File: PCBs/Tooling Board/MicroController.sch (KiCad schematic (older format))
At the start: 21 parts

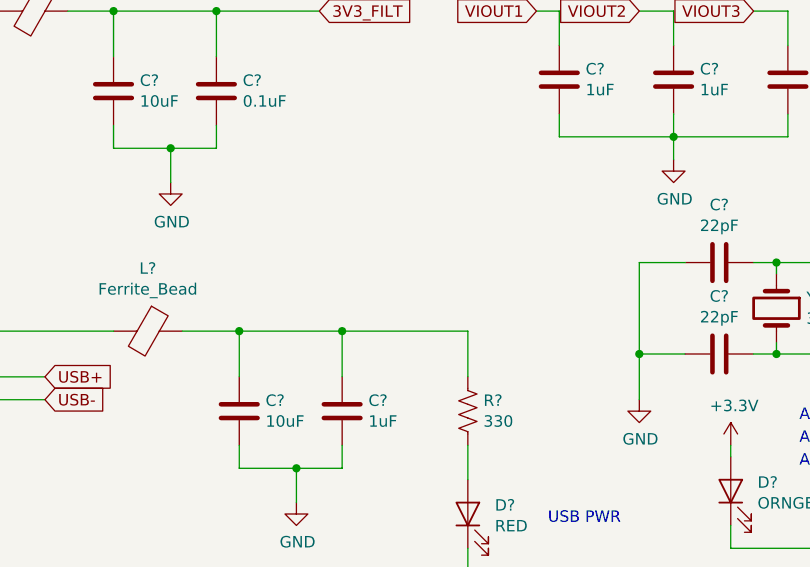
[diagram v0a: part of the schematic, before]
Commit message: Add DC Motor Control
-Added H-bridge drivers and logic inverters
-Should be able to control up to 6 DC motors / other loads
-We'll see if we can fit 3 chips on the board (we should be able to)
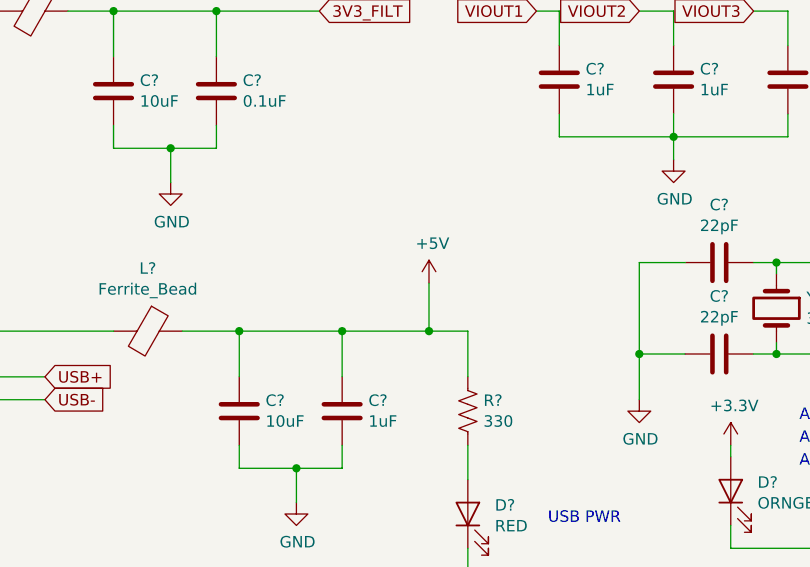
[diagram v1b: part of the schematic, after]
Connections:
- net +5V: now also C?.1, C?.1, L?.1, R?.1
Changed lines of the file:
@@
 $Descr A4 11693 8268
 encoding utf-8
-Sheet 2 4
+Sheet 2 7
 Title ""
 Date ""
@@
 Connection ~ 3250 2500
 Wire Wire Line
-	3250 2500 3800 2500
+	3250 2500 3630 2500
 Connection ~ 2800 2500
 Wire Wire Line
@@
 Text GLabel 5800 2850 0    50   Input ~ 0
 VIOUT1
+$Comp
+L power:+5V #PWR?
+U 1 1 5C4C3747
+P 3630 2290
+F 0 "#PWR?" H 3630 2140 50  0001 C CNN
+F 1 "+5V" H 3645 2463 50  0000 C CNN
+F 2 "" H 3630 2290 50  0001 C CNN
+F 3 "" H 3630 2290 50  0001 C CNN
+	1    3630 2290
+	1    0    0    -1
+$EndComp
+Wire Wire Line
+	3630 2290 3630 2500
+Connection ~ 3630 2500
+Wire Wire Line
+	3630 2500 3800 2500
 $EndSCHEMATC

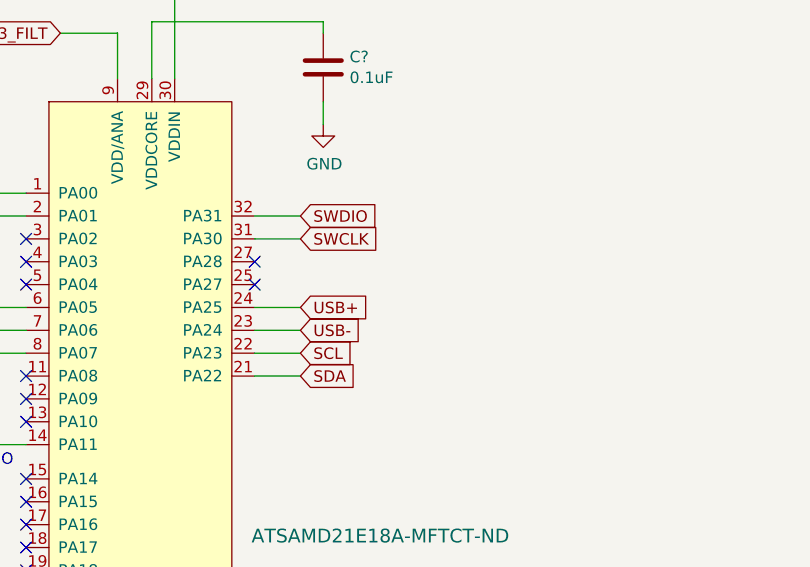
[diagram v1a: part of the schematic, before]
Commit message: Added Sensors
-Added pH Circuit and spec'd components
-Added Pressure sensor connecter
-Added External Temp sensor connector
-Added metal detector connector + input circuit

Need to add IMU interface now (not hard)
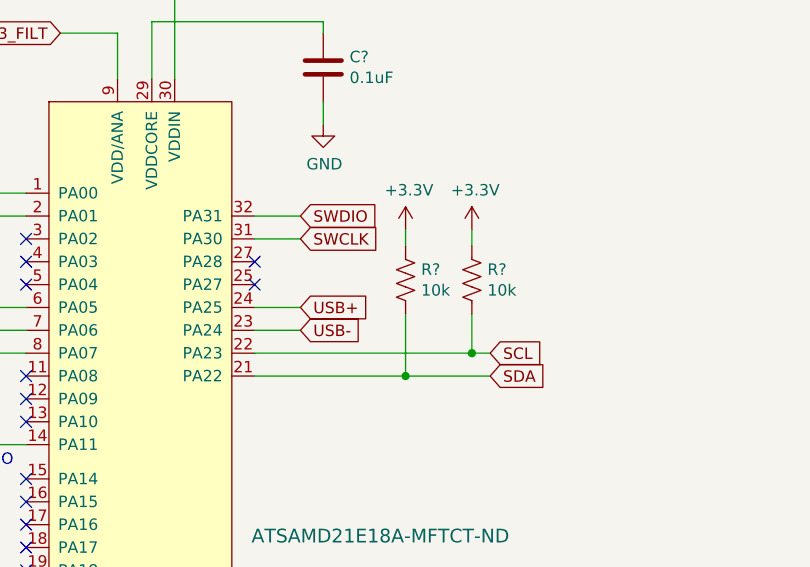
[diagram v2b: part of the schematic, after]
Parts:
- added R? (x2): 10k, symbol Device:R_US
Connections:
- net +3V3: now also R?.1, R?.1
- net SCL: now also R?.2
- net SDA: now also R?.2
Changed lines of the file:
@@
 $Descr A4 11693 8268
 encoding utf-8
-Sheet 2 7
+Sheet 2 8
 Title ""
 Date ""
@@
 	6000 3050 5800 3050
 Wire Wire Line
-	7000 3150 7200 3150
+	7000 3150 7660 3150
 Wire Wire Line
-	7000 3050 7200 3050
-Text GLabel 7200 3150 2    50   Input ~ 0
+	7000 3050 7950 3050
+Text GLabel 8030 3150 2    50   Input ~ 0
 SDA
-Text GLabel 7200 3050 2    50   Input ~ 0
+Text GLabel 8030 3050 2    50   Input ~ 0
 SCL
 $Comp
@@
 Wire Wire Line
 	3630 2500 3800 2500
+Wire Wire Line
+	7660 3150 7660 2880
+Connection ~ 7660 3150
+Wire Wire Line
+	7660 3150 8030 3150
+Wire Wire Line
+	7950 3050 7950 2880
+Connection ~ 7950 3050
+Wire Wire Line
+	7950 3050 8030 3050
+$Comp
+L Device:R_US R?
+U 1 1 5C4EC3B3
+P 7660 2730
+F 0 "R?" H 7728 2776 50  0000 L CNN
+F 1 "10k" H 7728 2685 50  0000 L CNN
+F 2 "" V 7700 2720 50  0001 C CNN
+F 3 "" H 7660 2730 50  0001 C CNN
+	1    7660 2730
+	1    0    0    -1
+$EndComp
+$Comp
+L Device:R_US R?
+U 1 1 5C4F7260
+P 7950 2730
+F 0 "R?" H 8018 2776 50  0000 L CNN
+F 1 "10k" H 8018 2685 50  0000 L CNN
+F 2 "" V 7990 2720 50  0001 C CNN
+F 3 "" H 7950 2730 50  0001 C CNN
+	1    7950 2730
+	1    0    0    -1
+$EndComp
+$Comp
+L power:+3.3V #PWR?
+U 1 1 5C4F72E4
+P 7660 2510
+F 0 "#PWR?" H 7660 2360 50  0001 C CNN
+F 1 "+3.3V" H 7675 2683 50  0000 C CNN
+F 2 "" H 7660 2510 50  0001 C CNN
+F 3 "" H 7660 2510 50  0001 C CNN
+	1    7660 2510
+	1    0    0    -1
+$EndComp
+$Comp
+L power:+3.3V #PWR?
+U 1 1 5C4F73BE
+P 7950 2510
+F 0 "#PWR?" H 7950 2360 50  0001 C CNN
+F 1 "+3.3V" H 7965 2683 50  0000 C CNN
+F 2 "" H 7950 2510 50  0001 C CNN
+F 3 "" H 7950 2510 50  0001 C CNN
+	1    7950 2510
+	1    0    0    -1
+$EndComp
+Wire Wire Line
+	7950 2580 7950 2510
+Wire Wire Line
+	7660 2580 7660 2510
 $EndSCHEMATC

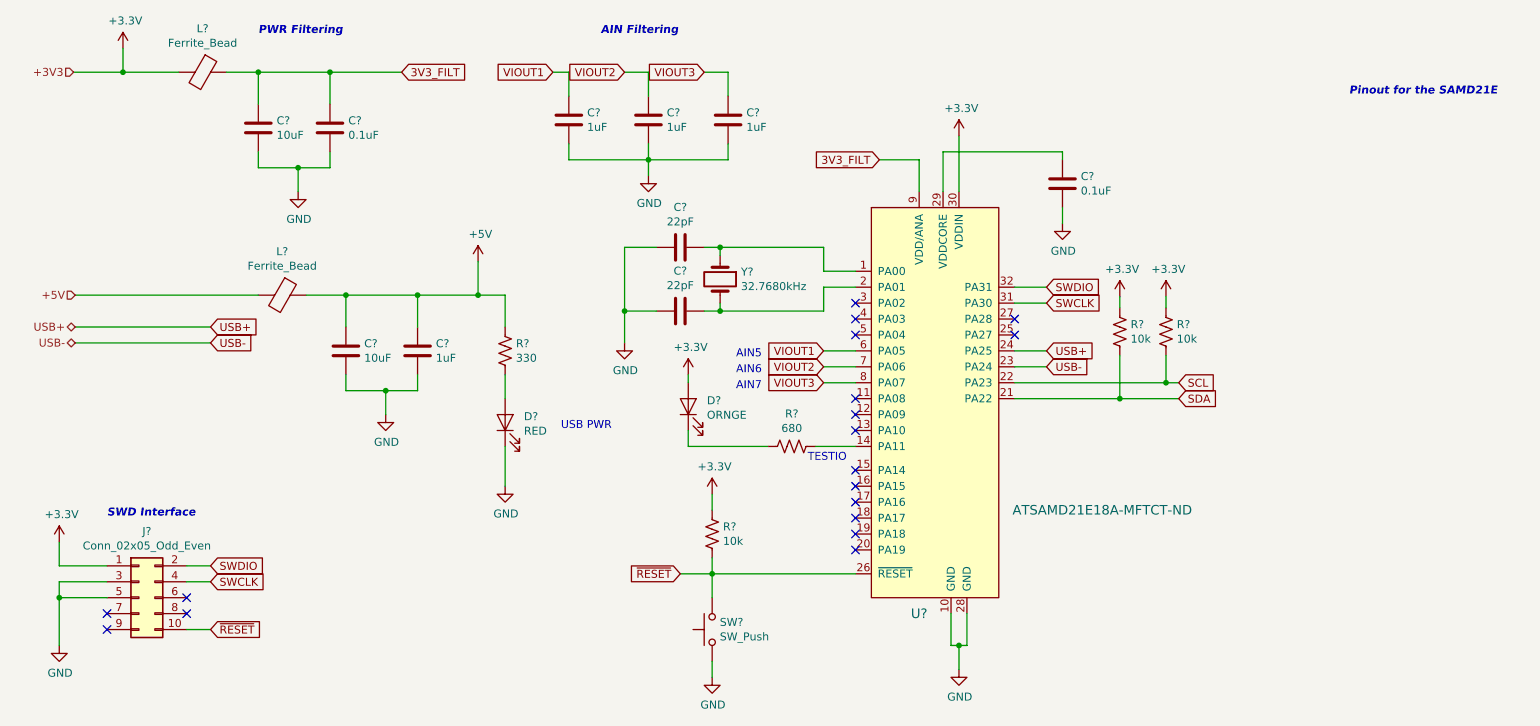
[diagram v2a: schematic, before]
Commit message: Pins are Mapped
-This was really difficult and it may not work.
-We're gonna try it and see what works.
-If it fails the next PCB will use arduino atmega chips since the open source libraries exist for them
-Might do a combination of SAMD and atmega lol
-God damn chinese new year
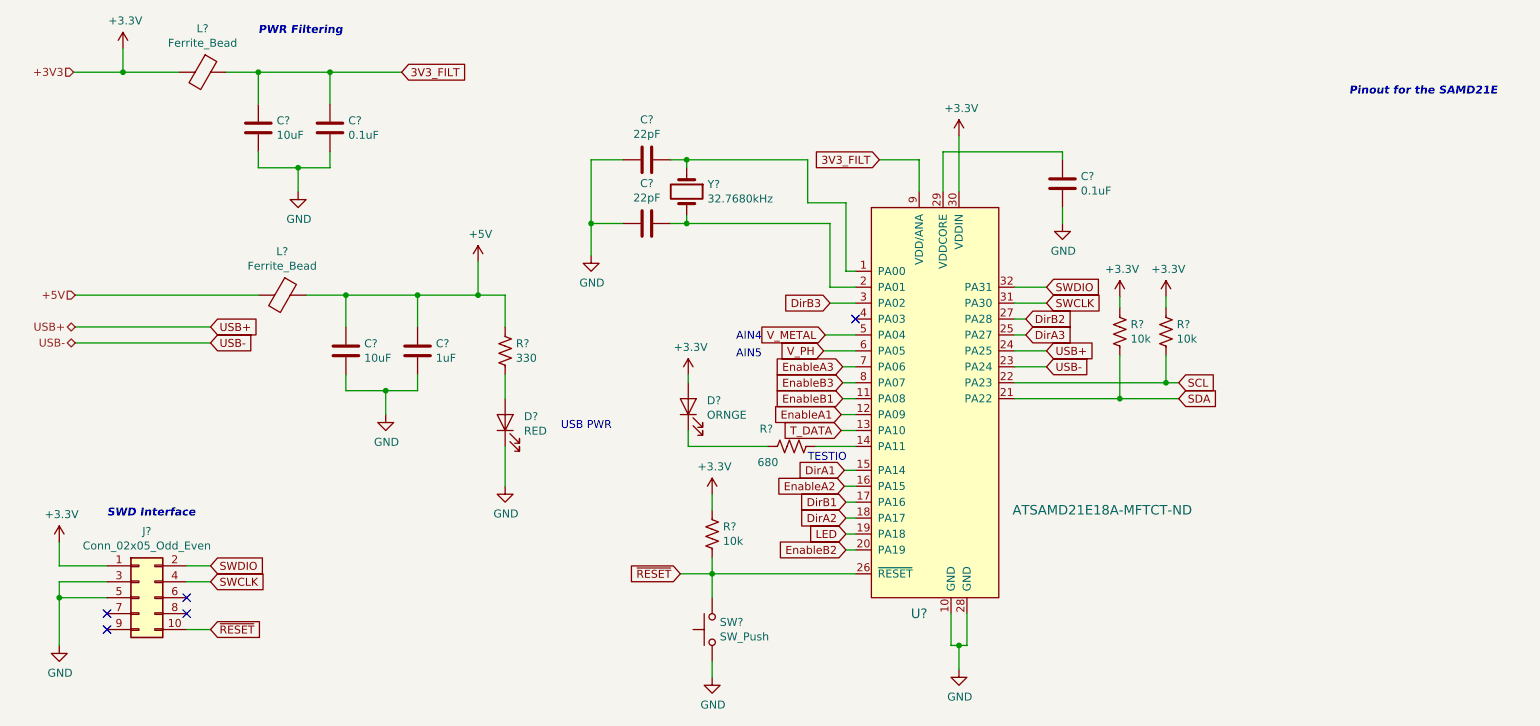
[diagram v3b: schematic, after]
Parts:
- removed C? (x3): 1uF, Capacitors_SMD:C_0603, symbol Device:C
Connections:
- net EnableB1: now reaches U?.11 (PA08)
- net EnableA1: now reaches U?.12 (PA09)
- net T_DATA: now reaches U?.13 (PA10)
- net DirA1: now reaches U?.15 (PA14)
- net EnableA2: now reaches U?.16 (PA15)
- net DirB1: now reaches U?.17 (PA16)
- net DirA2: now reaches U?.18 (PA17)
- net LED: now reaches U?.19 (PA18)
- net EnableB2: now reaches U?.20 (PA19)
- net DirA3: now reaches U?.25 (PA27)
- net DirB2: now reaches U?.27 (PA28)
- net DirB3: now reaches U?.3 (PA02)
- net V_METAL: now reaches U?.5 (PA04)
- net VIOUT1 renamed V_PH
- net VIOUT2 renamed EnableA3
- net VIOUT3 renamed EnableB3
- no-connect marks 18 -> 5
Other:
- note added: "AIN4"
- note removed: "AIN Filtering\n\n"
- note removed: "AIN6"
- note removed: "AIN7"
- moved on the sheet: C?, Y?
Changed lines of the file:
@@
 EESchema Schematic File Version 4
-LIBS:Actuator Board-cache
+LIBS:Tooling Board-cache
 EELAYER 26 0
 EELAYER END
@@
 Comment4 ""
 $EndDescr
-$Comp
-L EER:ATSAMD21E18A-MFT U?
-U 1 1 5BCD2DFE
-P 6500 3450
-F 0 "U?" H 6400 2400 60  0000 C CNN
-F 1 "ATSAMD21E18A-MFTCT-ND" H 7550 3050 60  0000 C CNN
-F 2 "EER:QFN-32-1EP_5x5mm" H 7900 3550 60  0001 L CNN
-F 3 "ATSAMD21E18A-MFTCT-ND" H 7900 3650 60  0001 L CNN
-F 4 "Active" H 6700 4650 60  0001 L CNN "Status"
-	1    6500 3450
-	1    0    0    -1
-$EndComp
 $Bitmap
 Pos 9600 3100
@@
 L Device:Crystal Y?
 U 1 1 5BDACFC8
-P 5150 2400
-F 0 "Y?" V 5104 2531 50  0000 L CNN
-F 1 "32.7680kHz" V 5195 2531 50  0000 L CNN
-F 2 "EER:Crystal_SMD_3215-2pin_3.2x1.5mm" H 5150 2400 50  0001 C CNN
-F 3 "887-2605-1-ND" H 5150 2400 50  0001 C CNN
-	1    5150 2400
+P 4940 1850
+F 0 "Y?" V 4894 1981 50  0000 L CNN
+F 1 "32.7680kHz" V 4985 1981 50  0000 L CNN
+F 2 "EER:Crystal_SMD_3215-2pin_3.2x1.5mm" H 4940 1850 50  0001 C CNN
+F 3 "887-2605-1-ND" H 4940 1850 50  0001 C CNN
+	1    4940 1850
 	0    1    1    0
 $EndComp
@@
 L Device:C C?
 U 1 1 5BDAD072
-P 4900 2200
-F 0 "C?" V 4648 2200 50  0000 C CNN
-F 1 "22pF" V 4739 2200 50  0000 C CNN
-F 2 "Capacitors_SMD:C_0603" H 4938 2050 50  0001 C CNN
-F 3 "311-3925-1-ND" H 4900 2200 50  0001 C CNN
-	1    4900 2200
+P 4690 1650
+F 0 "C?" V 4438 1650 50  0000 C CNN
+F 1 "22pF" V 4529 1650 50  0000 C CNN
+F 2 "Capacitors_SMD:C_0603" H 4728 1500 50  0001 C CNN
+F 3 "311-3925-1-ND" H 4690 1650 50  0001 C CNN
+	1    4690 1650
 	0    1    1    0
 $EndComp
@@
 L Device:C C?
 U 1 1 5BDAD111
-P 4900 2600
-F 0 "C?" V 4648 2600 50  0000 C CNN
-F 1 "22pF" V 4739 2600 50  0000 C CNN
-F 2 "Capacitors_SMD:C_0603" H 4938 2450 50  0001 C CNN
-F 3 "311-3925-1-ND" H 4900 2600 50  0001 C CNN
-	1    4900 2600
+P 4690 2050
+F 0 "C?" V 4438 2050 50  0000 C CNN
+F 1 "22pF" V 4529 2050 50  0000 C CNN
+F 2 "Capacitors_SMD:C_0603" H 4728 1900 50  0001 C CNN
+F 3 "311-3925-1-ND" H 4690 2050 50  0001 C CNN
+	1    4690 2050
 	0    1    1    0
 $EndComp
 Wire Wire Line
-	5050 2200 5150 2200
-Wire Wire Line
-	5150 2200 5150 2250
-Wire Wire Line
-	5150 2550 5150 2600
-Wire Wire Line
-	5150 2600 5050 2600
-Wire Wire Line
-	5150 2200 5800 2200
-Wire Wire Line
-	5800 2200 5800 2350
+	4840 1650 4940 1650
 Wire Wire Line
-	5800 2350 6000 2350
-Connection ~ 5150 2200
+	4940 1650 4940 1700
 Wire Wire Line
-	6000 2450 5800 2450
+	4940 2000 4940 2050
 Wire Wire Line
-	5800 2450 5800 2600
+	4940 2050 4840 2050
+Connection ~ 4940 1650
+Connection ~ 4940 2050
 Wire Wire Line
-	5800 2600 5150 2600
-Connection ~ 5150 2600
+	4540 1650 4340 1650
 Wire Wire Line
-	4750 2200 4550 2200
+	4340 1650 4340 2050
 Wire Wire Line
-	4550 2200 4550 2600
+	4340 2050 4540 2050
 Wire Wire Line
-	4550 2600 4750 2600
-Wire Wire Line
-	4550 2600 4550 2800
-Connection ~ 4550 2600
+	4340 2050 4340 2250
+Connection ~ 4340 2050
 $Comp
 L power:GND #PWR?
 U 1 1 5BDB1CC8
-P 4550 2800
-F 0 "#PWR?" H 4550 2550 50  0001 C CNN
-F 1 "GND" H 4555 2627 50  0000 C CNN
-F 2 "" H 4550 2800 50  0001 C CNN
-F 3 "" H 4550 2800 50  0001 C CNN
-	1    4550 2800
+P 4340 2250
+F 0 "#PWR?" H 4340 2000 50  0001 C CNN
+F 1 "GND" H 4345 2077 50  0000 C CNN
+F 2 "" H 4340 2250 50  0001 C CNN
+F 3 "" H 4340 2250 50  0001 C CNN
+	1    4340 2250
 	1    0    0    -1
 $EndComp
@@
 	6000 2850 5800 2850
 Wire Wire Line
-	6000 2950 5800 2950
-Wire Wire Line
-	6000 3050 5800 3050
-Wire Wire Line
 	7000 3150 7660 3150
 Wire Wire Line
@@
 U 1 1 5BDD760F
 P 5600 3450
-F 0 "R?" V 5395 3450 50  0000 C CNN
-F 1 "680" V 5486 3450 50  0000 C CNN
+F 0 "R?" V 5490 3290 50  0000 C CNN
+F 1 "680" V 5700 3300 50  0000 C CNN
 F 2 "Resistors_SMD:R_0603" V 5640 3440 50  0001 C CNN
 F 3 "RHM680DCT-ND" H 5600 3450 50  0001 C CNN
@@
 Wire Wire Line
 	5100 4250 6000 4250
-NoConn ~ 6000 2550
-NoConn ~ 6000 2650
-NoConn ~ 6000 2750
-NoConn ~ 6000 3150
-NoConn ~ 6000 3250
-NoConn ~ 6000 3350
-NoConn ~ 6000 3600
-NoConn ~ 6000 3700
-NoConn ~ 6000 3800
-NoConn ~ 6000 4000
-NoConn ~ 6000 3900
-NoConn ~ 6000 4100
-NoConn ~ 7000 2750
-NoConn ~ 7000 2650
 Text Notes 2250 950  0    50   Italic 10
 PWR Filtering\n\n
@@
 NoConn ~ 1300 4500
 NoConn ~ 1300 4600
-$Comp
-L Device:C C?
-U 1 1 5BE103F1
-P 4200 1400
-F 0 "C?" H 4315 1446 50  0000 L CNN
-F 1 "1uF" H 4315 1355 50  0000 L CNN
-F 2 "Capacitors_SMD:C_0603" H 4238 1250 50  0001 C CNN
-F 3 "1276-6524-1-ND" H 4200 1400 50  0001 C CNN
-	1    4200 1400
-	1    0    0    -1
-$EndComp
-$Comp
-L Device:C C?
-U 1 1 5BE1047D
-P 4700 1400
-F 0 "C?" H 4815 1446 50  0000 L CNN
-F 1 "1uF" H 4815 1355 50  0000 L CNN
-F 2 "Capacitors_SMD:C_0603" H 4738 1250 50  0001 C CNN
-F 3 "1276-6524-1-ND" H 4700 1400 50  0001 C CNN
-	1    4700 1400
-	1    0    0    -1
-$EndComp
-$Comp
-L Device:C C?
-U 1 1 5BE104C5
-P 5200 1400
-F 0 "C?" H 5315 1446 50  0000 L CNN
-F 1 "1uF" H 5315 1355 50  0000 L CNN
-F 2 "Capacitors_SMD:C_0603" H 5238 1250 50  0001 C CNN
-F 3 "1276-6524-1-ND" H 5200 1400 50  0001 C CNN
-	1    5200 1400
-	1    0    0    -1
-$EndComp
-Wire Wire Line
-	4200 1250 4200 1100
-Wire Wire Line
-	4700 1250 4700 1100
-Wire Wire Line
-	4700 1100 4550 1100
-Wire Wire Line
-	5200 1250 5200 1100
-Wire Wire Line
-	4200 1550 4200 1650
-Wire Wire Line
-	4200 1650 4700 1650
-Wire Wire Line
-	4700 1650 4700 1550
-Wire Wire Line
-	5200 1550 5200 1650
-Wire Wire Line
-	5200 1650 4700 1650
-Connection ~ 4700 1650
-Wire Wire Line
-	4700 1650 4700 1750
-$Comp
-L power:GND #PWR?
-U 1 1 5BE1E788
-P 4700 1750
-F 0 "#PWR?" H 4700 1500 50  0001 C CNN
-F 1 "GND" H 4705 1577 50  0000 C CNN
-F 2 "" H 4700 1750 50  0001 C CNN
-F 3 "" H 4700 1750 50  0001 C CNN
-	1    4700 1750
-	1    0    0    -1
-$EndComp
-Text GLabel 4100 1100 0    50   Input ~ 0
-VIOUT1
-Text GLabel 4550 1100 0    50   Input ~ 0
-VIOUT2
-Wire Wire Line
-	4200 1100 4100 1100
-Text GLabel 5050 1100 0    50   Input ~ 0
-VIOUT3
-Wire Wire Line
-	5050 1100 5200 1100
-Text Notes 4400 950  0    50   Italic 10
-AIN Filtering\n\n
 Wire Wire Line
 	1400 1100 1090 1100
@@
 Wire Wire Line
 	1100 2500 2250 2500
-Text Notes 5250 3100 0    50   ~ 0
-AIN7
-Text Notes 5250 3000 0    50   ~ 0
-AIN6
 Text Notes 5250 2900 0    50   ~ 0
 AIN5
-Text GLabel 5800 3050 0    50   Input ~ 0
-VIOUT3
-Text GLabel 5800 2950 0    50   Input ~ 0
-VIOUT2
-Text GLabel 5800 2850 0    50   Input ~ 0
-VIOUT1
 $Comp
 L power:+5V #PWR?
@@
 Wire Wire Line
 	7660 2580 7660 2510
+Text GLabel 5800 2850 0    50   Input ~ 0
+V_PH
+Text GLabel 5810 2750 0    50   Input ~ 0
+V_METAL
+Wire Wire Line
+	5700 1650 5700 1920
+Wire Wire Line
+	5700 1920 5940 1920
+Wire Wire Line
+	5940 1920 5940 2350
+Wire Wire Line
+	5940 2350 6000 2350
+Wire Wire Line
+	4940 1650 5700 1650
+Wire Wire Line
+	5840 2450 5840 2050
+Wire Wire Line
+	4940 2050 5840 2050
+Wire Wire Line
+	5840 2450 6000 2450
+Text GLabel 5910 3250 0    50   Input ~ 0
+EnableA1
+Wire Wire Line
+	5910 3250 6000 3250
+Text GLabel 5930 3600 0    50   Input ~ 0
+DirA1
+$Comp
+L EER:ATSAMD21E18A-MFT U?
+U 1 1 5BCD2DFE
+P 6500 3450
+F 0 "U?" H 6400 2400 60  0000 C CNN
+F 1 "ATSAMD21E18A-MFTCT-ND" H 7550 3050 60  0000 C CNN
+F 2 "EER:QFN-32-1EP_5x5mm" H 7900 3550 60  0001 L CNN
+F 3 "ATSAMD21E18A-MFTCT-ND" H 7900 3650 60  0001 L CNN
+F 4 "Active" H 6700 4650 60  0001 L CNN "Status"
+	1    6500 3450
+	1    0    0    -1
+$EndComp
+Text GLabel 5930 3700 0    50   Input ~ 0
+EnableA2
+Text GLabel 5940 3800 0    50   Input ~ 0
+DirB1
+Text GLabel 5940 4000 0    50   Input ~ 0
+LED
+Text GLabel 5940 4100 0    50   Input ~ 0
+EnableB2
+Text GLabel 5920 3150 0    50   Input ~ 0
+EnableB1
+Wire Wire Line
+	5920 3150 6000 3150
+Wire Wire Line
+	5930 3600 6000 3600
+Wire Wire Line
+	6000 3700 5930 3700
+Wire Wire Line
+	5940 3800 6000 3800
+Wire Wire Line
+	6000 3900 5940 3900
+Wire Wire Line
+	5940 4000 6000 4000
+Wire Wire Line
+	5940 4100 6000 4100
+Wire Wire Line
+	7000 2750 7070 2750
+Wire Wire Line
+	7000 2650 7070 2650
+Text GLabel 7070 2650 2    50   Input ~ 0
+DirB2
+Text GLabel 7070 2750 2    50   Input ~ 0
+DirA3
+Text GLabel 5920 2950 0    50   Input ~ 0
+EnableA3
+Text GLabel 5920 3050 0    50   Input ~ 0
+EnableB3
+Wire Wire Line
+	5920 3050 6000 3050
+Wire Wire Line
+	6000 2950 5920 2950
+Text GLabel 5940 3900 0    50   Input ~ 0
+DirA2
+Wire Wire Line
+	5810 2750 6000 2750
+Text GLabel 5840 2550 0    50   Input ~ 0
+DirB3
+Wire Wire Line
+	5840 2550 6000 2550
+NoConn ~ 6000 2650
+Wire Wire Line
+	6000 3350 5910 3350
+Text GLabel 5910 3350 0    50   Input ~ 0
+T_DATA
+Text Notes 5250 2790 0    50   ~ 0
+AIN4
 $EndSCHEMATC

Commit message: Added Footprints
-Whoooo boy here we go
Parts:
- C201, C202, C203, C204, C207: renamed from C?; footprint Capacitors_SMD:C_0603 -> Capacitors_SMD:C_0805_HandSoldering
- C205, C206: renamed from C?; footprint Capacitors_SMD:C_0603 -> Capacitors_SMD:C_0603_HandSoldering
- D201, D202: renamed from D?; footprint LEDs:LED_0805 -> LEDs:LED_0805_HandSoldering
- R201, R203: renamed from R?; footprint Resistors_SMD:R_0603 -> Resistors_SMD:R_0805_HandSoldering
- R202: renamed from R?; footprint Resistors_SMD:R_0805 -> Resistors_SMD:R_0805_HandSoldering
- R204, R205: renamed from R?; footprint (none) -> Resistors_SMD:R_0805_HandSoldering
- gave numbers to parts that had none: 6
